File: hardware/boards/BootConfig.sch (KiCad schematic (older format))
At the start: 27 parts, among them J3 Conn_02x05_Odd_Even, SW1 SW_DIP_x03, U1 ECP5UM5G-381caBGA, U3 CYUSB3014, U5 128MiB

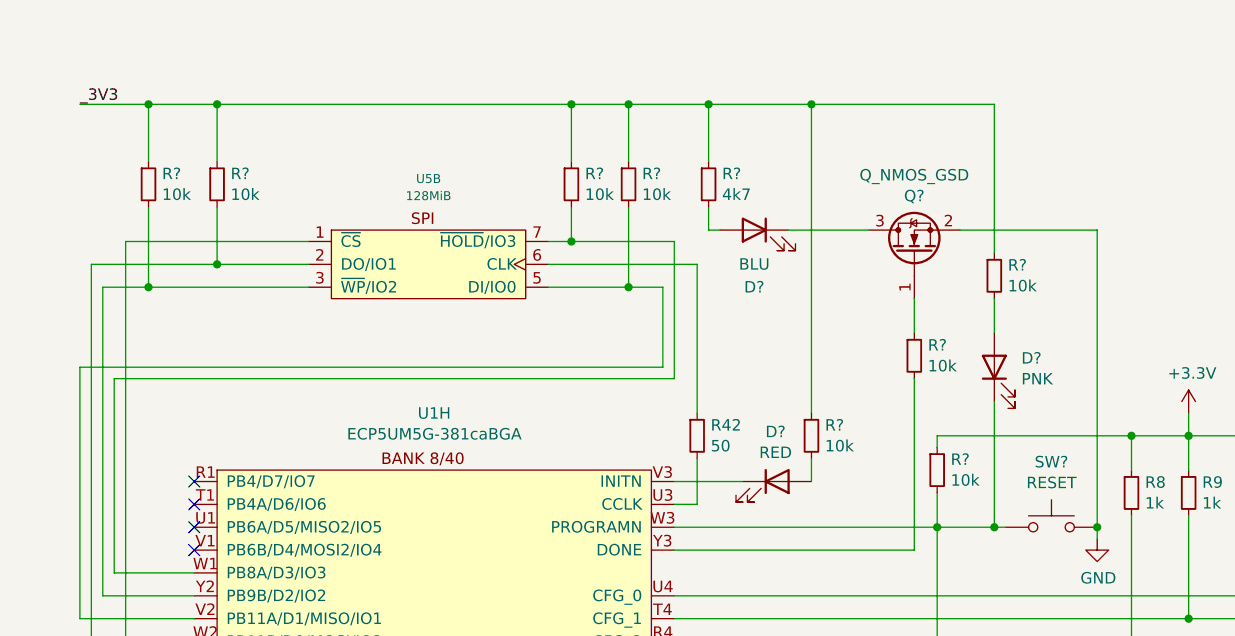
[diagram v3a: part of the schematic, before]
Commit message: Some ERC cleanup
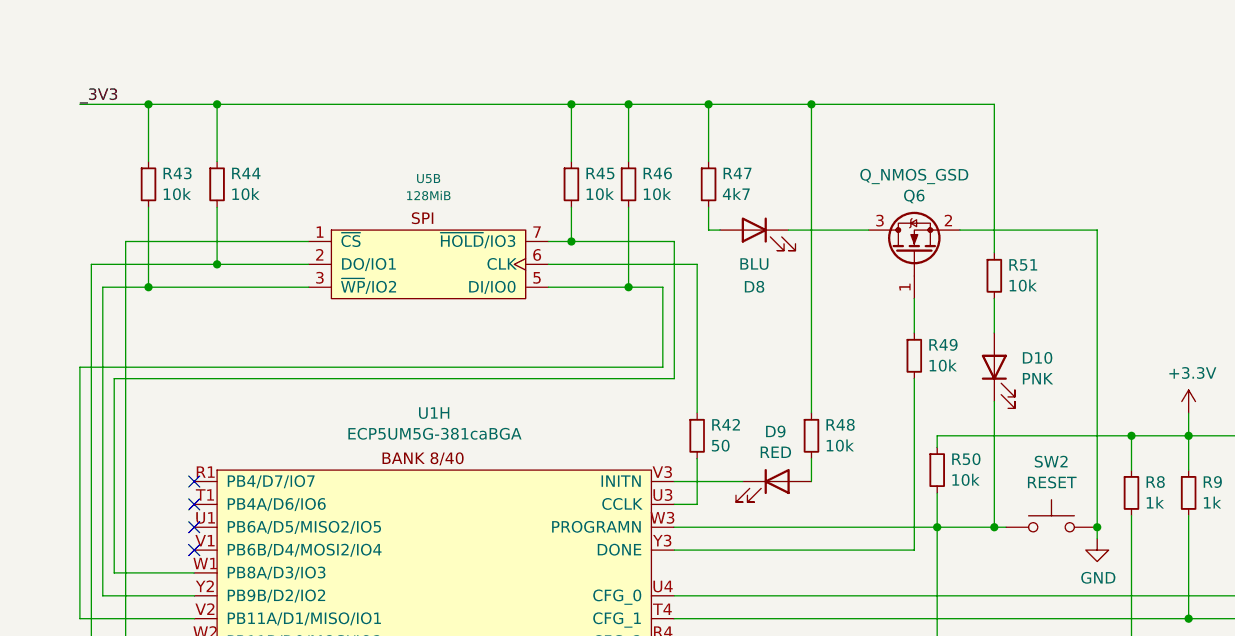
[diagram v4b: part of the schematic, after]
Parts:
- gave numbers to parts that had none: 14
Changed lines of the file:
@@
 	7400 4550 7400 4350
 $Comp
-L Switch:SW_Push SW?
+L Switch:SW_Push SW2
 U 1 1 5FFCED2D
 P 8950 4650
-F 0 "SW?" H 8950 4935 50  0000 C CNN
+F 0 "SW2" H 8950 4935 50  0000 C CNN
 F 1 "RESET" H 8950 4844 50  0000 C CNN
 F 2 "" H 8950 4850 50  0001 C CNN
@@
 P 5000 3150
 AR Path="/5EDF9F51/5FFF11C1" Ref="R?"  Part="1"
-AR Path="/5EF66251/5FFF11C1" Ref="R?"  Part="1"
-F 0 "R?" H 5059 3196 50  0000 L CNN
+AR Path="/5EF66251/5FFF11C1" Ref="R43"  Part="1"
+F 0 "R43" H 5059 3196 50  0000 L CNN
 F 1 "10k" H 5059 3105 50  0000 L CNN
 F 2 "Resistor_SMD:R_0603_1608Metric" H 5000 3150 50  0001 C CNN
@@
 P 5300 3150
 AR Path="/5EDF9F51/5FFF5085" Ref="R?"  Part="1"
-AR Path="/5EF66251/5FFF5085" Ref="R?"  Part="1"
-F 0 "R?" H 5359 3196 50  0000 L CNN
+AR Path="/5EF66251/5FFF5085" Ref="R44"  Part="1"
+F 0 "R44" H 5359 3196 50  0000 L CNN
 F 1 "10k" H 5359 3105 50  0000 L CNN
 F 2 "Resistor_SMD:R_0603_1608Metric" H 5300 3150 50  0001 C CNN
@@
 P 7100 3150
 AR Path="/5EDF9F51/5FFF5831" Ref="R?"  Part="1"
-AR Path="/5EF66251/5FFF5831" Ref="R?"  Part="1"
-F 0 "R?" H 7159 3196 50  0000 L CNN
+AR Path="/5EF66251/5FFF5831" Ref="R46"  Part="1"
+F 0 "R46" H 7159 3196 50  0000 L CNN
 F 1 "10k" H 7159 3105 50  0000 L CNN
 F 2 "Resistor_SMD:R_0603_1608Metric" H 7100 3150 50  0001 C CNN
@@
 P 6850 3150
 AR Path="/5EDF9F51/5FFF5FBB" Ref="R?"  Part="1"
-AR Path="/5EF66251/5FFF5FBB" Ref="R?"  Part="1"
-F 0 "R?" H 6909 3196 50  0000 L CNN
+AR Path="/5EF66251/5FFF5FBB" Ref="R45"  Part="1"
+F 0 "R45" H 6909 3196 50  0000 L CNN
 F 1 "10k" H 6909 3105 50  0000 L CNN
 F 2 "Resistor_SMD:R_0603_1608Metric" H 6850 3150 50  0001 C CNN
@@
 This should just be replaced with the proper\npull-ups/downs to statically configure,\nbut for rev 0 lets let it be configurable.
 $Comp
-L power:GND #PWR?
+L power:GND #PWR0128
 U 1 1 6021C990
 P 9150 4700
-F 0 "#PWR?" H 9150 4450 50  0001 C CNN
+F 0 "#PWR0128" H 9150 4450 50  0001 C CNN
 F 1 "GND" H 9155 4527 50  0000 C CNN
 F 2 "" H 9150 4700 50  0001 C CNN
@@
 P 8450 4400
 AR Path="/5EDF9F51/6022837B" Ref="R?"  Part="1"
-AR Path="/5EF66251/6022837B" Ref="R?"  Part="1"
-F 0 "R?" H 8509 4446 50  0000 L CNN
+AR Path="/5EF66251/6022837B" Ref="R50"  Part="1"
+F 0 "R50" H 8509 4446 50  0000 L CNN
 F 1 "10k" H 8509 4355 50  0000 L CNN
 F 2 "Resistor_SMD:R_0603_1608Metric" H 8450 4400 50  0001 C CNN
@@
 Connection ~ 9300 4250
 $Comp
-L Device:LED D?
+L Device:LED D10
 U 1 1 6023CC12
 P 8700 3950
-F 0 "D?" V 8739 3832 50  0000 R CNN
+F 0 "D10" V 8739 3832 50  0000 R CNN
 F 1 "PNK" V 8648 3832 50  0000 R CNN
 F 2 "LED_SMD:LED_0603_1608Metric" H 8700 3950 50  0001 C CNN
@@
 P 8700 3550
 AR Path="/5EDF9F51/6025A141" Ref="R?"  Part="1"
-AR Path="/5EF66251/6025A141" Ref="R?"  Part="1"
-F 0 "R?" H 8759 3596 50  0000 L CNN
+AR Path="/5EF66251/6025A141" Ref="R51"  Part="1"
+F 0 "R51" H 8759 3596 50  0000 L CNN
 F 1 "10k" H 8759 3505 50  0000 L CNN
 F 2 "Resistor_SMD:R_0603_1608Metric" H 8700 3550 50  0001 C CNN
@@
 Connection ~ 7100 2800
 $Comp
-L Device:LED D?
+L Device:LED D9
 U 1 1 60311968
 P 7750 4450
-F 0 "D?" H 7743 4667 50  0000 C CNN
+F 0 "D9" H 7743 4667 50  0000 C CNN
 F 1 "RED" H 7743 4576 50  0000 C CNN
 F 2 "LED_SMD:LED_0603_1608Metric" H 7750 4450 50  0001 C CNN
@@
 P 7900 4250
 AR Path="/5EDF9F51/60331B52" Ref="R?"  Part="1"
-AR Path="/5EF66251/60331B52" Ref="R?"  Part="1"
-F 0 "R?" H 7959 4296 50  0000 L CNN
+AR Path="/5EF66251/60331B52" Ref="R48"  Part="1"
+F 0 "R48" H 7959 4296 50  0000 L CNN
 F 1 "10k" H 7959 4205 50  0000 L CNN
 F 2 "Resistor_SMD:R_0603_1608Metric" H 7900 4250 50  0001 C CNN
@@
 P 8350 3450
 AR Path="/5EDF9F51/6036E4C5" Ref="Q?"  Part="1"
-AR Path="/5EF66251/6036E4C5" Ref="Q?"  Part="1"
-F 0 "Q?" V 8599 3450 50  0000 C CNN
+AR Path="/5EF66251/6036E4C5" Ref="Q6"  Part="1"
+F 0 "Q6" V 8599 3450 50  0000 C CNN
 F 1 "Q_NMOS_GSD" V 8690 3450 50  0000 C CNN
 F 2 "Package_TO_SOT_SMD:SOT-23" H 8550 3550 50  0001 C CNN
@@
 Connection ~ 9150 4650
 $Comp
-L Device:LED D?
+L Device:LED D8
 U 1 1 603DB6B8
 P 7650 3350
-F 0 "D?" H 7650 3100 50  0000 C CNN
+F 0 "D8" H 7650 3100 50  0000 C CNN
 F 1 "BLU" H 7650 3200 50  0000 C CNN
 F 2 "LED_SMD:LED_0603_1608Metric" H 7650 3350 50  0001 C CNN
@@
 P 7450 3150
 AR Path="/5EDF9F51/603E9951" Ref="R?"  Part="1"
-AR Path="/5EF66251/603E9951" Ref="R?"  Part="1"
-F 0 "R?" H 7509 3196 50  0000 L CNN
+AR Path="/5EF66251/603E9951" Ref="R47"  Part="1"
+F 0 "R47" H 7509 3196 50  0000 L CNN
 F 1 "4k7" H 7509 3105 50  0000 L CNN
 F 2 "Resistor_SMD:R_0603_1608Metric" H 7450 3150 50  0001 C CNN
@@
 P 8350 3900
 AR Path="/5EDF9F51/604133D3" Ref="R?"  Part="1"
-AR Path="/5EF66251/604133D3" Ref="R?"  Part="1"
-F 0 "R?" H 8409 3946 50  0000 L CNN
+AR Path="/5EF66251/604133D3" Ref="R49"  Part="1"
+F 0 "R49" H 8409 3946 50  0000 L CNN
 F 1 "10k" H 8409 3855 50  0000 L CNN
 F 2 "Resistor_SMD:R_0603_1608Metric" H 8350 3900 50  0001 C CNN

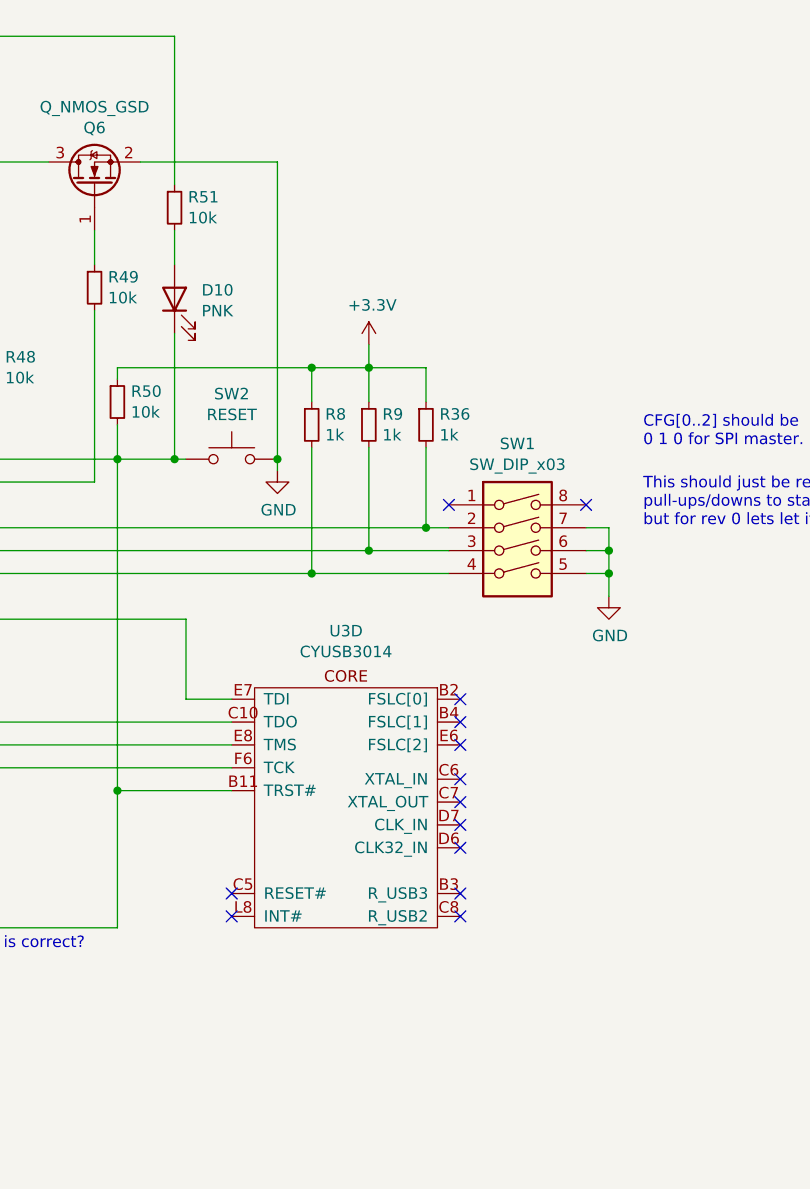
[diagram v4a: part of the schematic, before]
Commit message: Added a debounce cap to the reset switch, as well as selected the reset switch itself, also added the needed pull-down resistors for the USB PHY
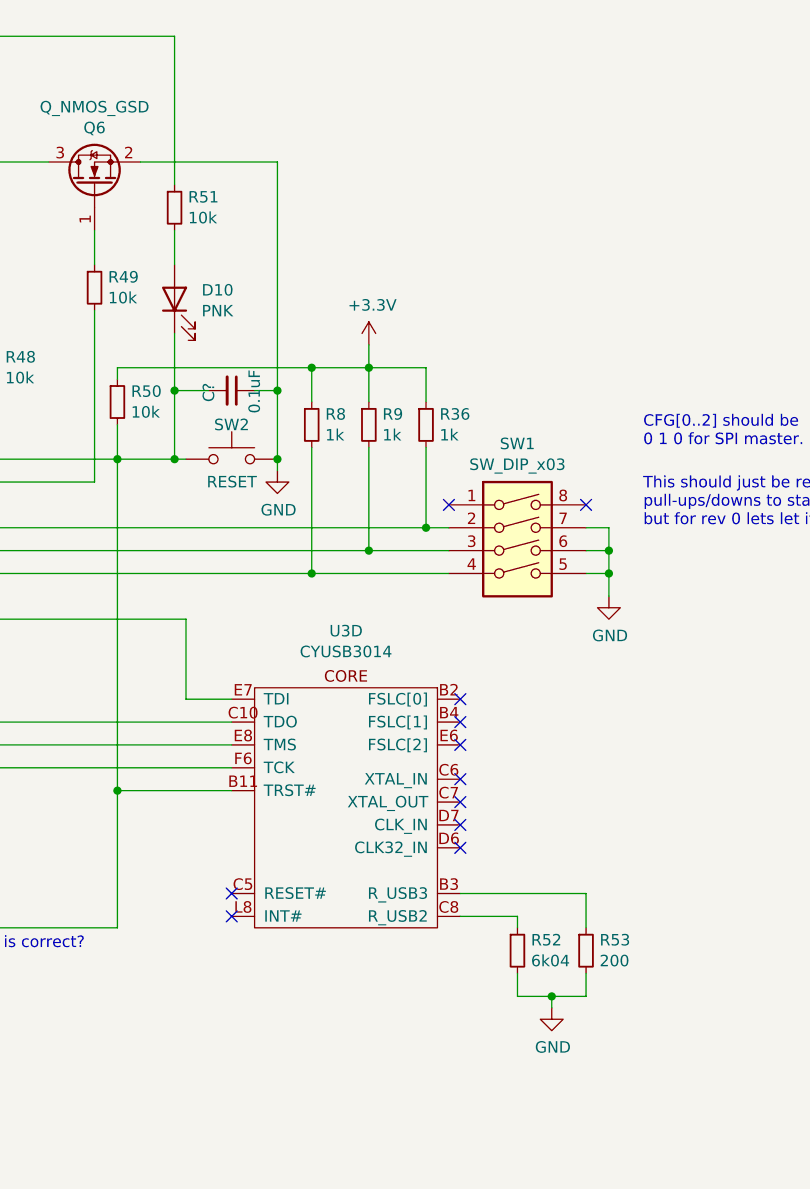
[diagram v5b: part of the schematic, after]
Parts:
- added C?: 0.1uF, Capacitor_SMD:C_0603_1608Metric, symbol Device:C_Small
- added R52: 6k04, Resistor_SMD:R_0603_1608Metric, symbol Device:R_Small
- added R53: 200, Resistor_SMD:R_0603_1608Metric, symbol Device:R_Small
- SW2: footprint (none) -> Button_Switch_SMD:SW_Push_1P1T_NO_CK_KMR2; MFR (none) -> C&K; MPN (none) -> KMR241NG ULC LFS
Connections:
- net GND: now also C?.1, R52.2, R53.2
- net at D10.1 (K), J3.10 (Pin_10), R50.2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: now also C?.2
- net at U3.B3 (R_USB3): now also R53.1
- net at U3.C8 (R_USB2): now also R52.1
- no-connect marks 22 -> 20
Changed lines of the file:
@@
 NoConn ~ 9950 6250
 NoConn ~ 9950 6350
-NoConn ~ 9950 6550
-NoConn ~ 9950 6650
 NoConn ~ 8950 6650
 NoConn ~ 8950 6550
@@
 U 1 1 5FFCED2D
 P 8950 4650
-F 0 "SW2" H 8950 4935 50  0000 C CNN
-F 1 "RESET" H 8950 4844 50  0000 C CNN
-F 2 "" H 8950 4850 50  0001 C CNN
-F 3 "~" H 8950 4850 50  0001 C CNN
+F 0 "SW2" H 8950 4800 50  0000 C CNN
+F 1 "RESET" H 8950 4550 50  0000 C CNN
+F 2 "Button_Switch_SMD:SW_Push_1P1T_NO_CK_KMR2" H 8950 4850 50  0001 C CNN
+F 3 "https://www.ckswitches.com/media/1479/kmr2.pdf" H 8950 4850 50  0001 C CNN
+F 4 "C&K" H 8950 4650 50  0001 C CNN "MFR"
+F 5 "KMR241NG ULC LFS" H 8950 4650 50  0001 C CNN "MPN"
 	1    8950 4650
 	1    0    0    -1
@@
 $EndComp
 Wire Wire Line
-	8700 4100 8700 4650
+	8700 4100 8700 4350
 Connection ~ 8700 4650
 Wire Wire Line
@@
 	8550 3350 9150 3350
 Wire Wire Line
-	9150 3350 9150 4650
+	9150 3350 9150 4350
 Connection ~ 9150 4650
 $Comp
@@
 Wire Wire Line
 	8450 6100 8450 4650
+$Comp
+L Device:R_Small R52
+U 1 1 60672CB4
+P 10200 6800
+F 0 "R52" H 10259 6846 50  0000 L CNN
+F 1 "6k04" H 10259 6755 50  0000 L CNN
+F 2 "Resistor_SMD:R_0603_1608Metric" H 10200 6800 50  0001 C CNN
+F 3 "~" H 10200 6800 50  0001 C CNN
+F 4 "Vishay Dale" H 10200 6800 50  0001 C CNN "MFR"
+F 5 "RCS06036K04FKEA" H 10200 6800 50  0001 C CNN "MPN"
+	1    10200 6800
+	1    0    0    -1
+$EndComp
+$Comp
+L Device:R_Small R53
+U 1 1 6067E54E
+P 10500 6800
+F 0 "R53" H 10559 6846 50  0000 L CNN
+F 1 "200" H 10559 6755 50  0000 L CNN
+F 2 "Resistor_SMD:R_0603_1608Metric" H 10500 6800 50  0001 C CNN
+F 3 "~" H 10500 6800 50  0001 C CNN
+F 4 "Vishay Dale" H 10500 6800 50  0001 C CNN "MFR"
+F 5 "RCS0603200RFKEA" H 10500 6800 50  0001 C CNN "MPN"
+	1    10500 6800
+	1    0    0    -1
+$EndComp
+Wire Wire Line
+	9950 6650 10200 6650
+Wire Wire Line
+	10200 6650 10200 6700
+Wire Wire Line
+	9950 6550 10500 6550
+Wire Wire Line
+	10500 6550 10500 6700
+$Comp
+L power:GND #PWR0129
+U 1 1 6068AA91
+P 10350 7050
+F 0 "#PWR0129" H 10350 6800 50  0001 C CNN
+F 1 "GND" H 10355 6877 50  0000 C CNN
+F 2 "" H 10350 7050 50  0001 C CNN
+F 3 "" H 10350 7050 50  0001 C CNN
+	1    10350 7050
+	1    0    0    -1
+$EndComp
+Wire Wire Line
+	10200 6900 10200 7000
+Wire Wire Line
+	10200 7000 10350 7000
+Wire Wire Line
+	10350 7000 10350 7050
+Wire Wire Line
+	10500 6900 10500 7000
+Wire Wire Line
+	10500 7000 10350 7000
+Connection ~ 10350 7000
+$Comp
+L Device:C_Small C?
+U 1 1 606E230C
+P 8950 4350
+AR Path="/5EDF9F51/606E230C" Ref="C?"  Part="1"
+AR Path="/5EF66251/606E230C" Ref="C?"  Part="1"
+F 0 "C?" H 9000 4250 50  0000 R CNN
+F 1 "0.1uF" H 9050 4450 50  0000 R CNN
+F 2 "Capacitor_SMD:C_0603_1608Metric" H 8950 4350 50  0001 C CNN
+F 3 "~" H 8950 4350 50  0001 C CNN
+F 4 "KEMET" V 8950 4350 50  0001 C CNN "MFR"
+F 5 "C0603C104M5RACTU" V 8950 4350 50  0001 C CNN "MPN"
+	1    8950 4350
+	0    1    1    0
+$EndComp
+Wire Wire Line
+	8700 4350 8850 4350
+Connection ~ 8700 4350
+Wire Wire Line
+	8700 4350 8700 4650
+Wire Wire Line
+	9050 4350 9150 4350
+Connection ~ 9150 4350
+Wire Wire Line
+	9150 4350 9150 4650
 $EndSCHEMATC

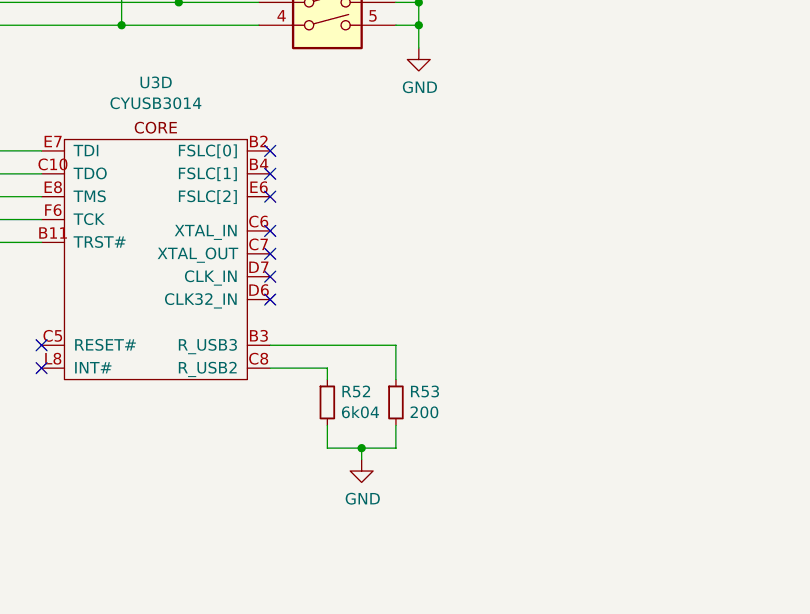
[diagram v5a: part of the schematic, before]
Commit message: Added the crystal for the USB PHY
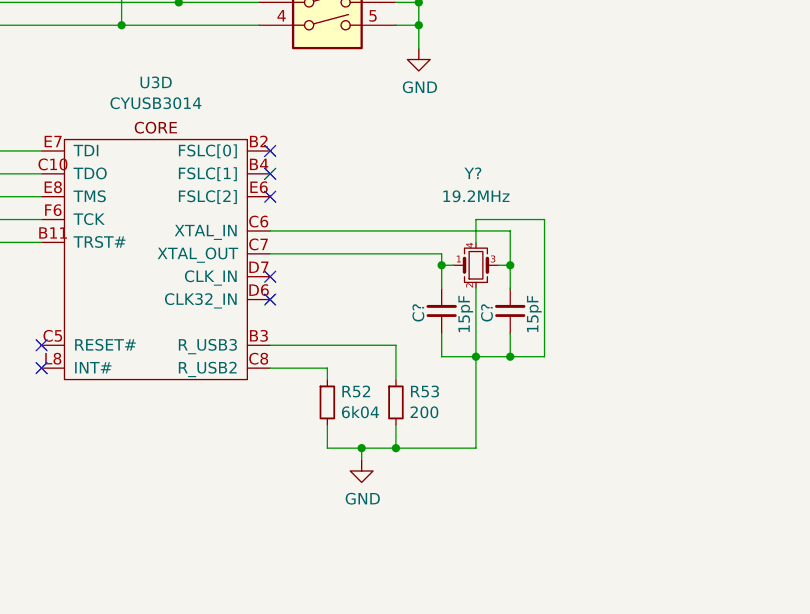
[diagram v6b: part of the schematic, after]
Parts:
- added C? (x2): 15pF, Capacitor_SMD:C_0603_1608Metric, symbol Device:C_Small
- added Y?: 19.2MHz, Crystal:Crystal_SMD_Abracon_ABM10-4Pin_2.5x2.0mm, symbol Device:Crystal_GND24_Small
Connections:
- net GND: now also C?.1, C?.1, Y?.2, Y?.4
- net at U3.C6 (XTAL_IN): now also C?.2, Y?.3
- net at U3.C7 (XTAL_OUT): now also C?.2, Y?.1
- no-connect marks 20 -> 18
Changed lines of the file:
@@
 NoConn ~ 9950 5800
 NoConn ~ 9950 5900
-NoConn ~ 9950 6050
-NoConn ~ 9950 6150
 NoConn ~ 9950 6250
 NoConn ~ 9950 6350
@@
 Wire Wire Line
 	9150 4350 9150 4650
+$Comp
+L Device:Crystal_GND24_Small Y?
+U 1 1 6071D344
+P 10850 6200
+F 0 "Y?" H 10800 6600 50  0000 L CNN
+F 1 "19.2MHz" H 10700 6500 50  0000 L CNN
+F 2 "Crystal:Crystal_SMD_Abracon_ABM10-4Pin_2.5x2.0mm" H 10850 6200 50  0001 C CNN
+F 3 "~" H 10850 6200 50  0001 C CNN
+F 4 "Abracon LLC" H 10850 6200 50  0001 C CNN "MFR"
+F 5 "ABM10-19.200MHZ-D30-T3" H 10850 6200 50  0001 C CNN "MPN"
+	1    10850 6200
+	1    0    0    -1
+$EndComp
+$Comp
+L Device:C_Small C?
+U 1 1 60727D1B
+P 10700 6400
+AR Path="/5EDF9F51/60727D1B" Ref="C?"  Part="1"
+AR Path="/5EF66251/60727D1B" Ref="C?"  Part="1"
+F 0 "C?" V 10800 6450 50  0000 R CNN
+F 1 "15pF" V 10600 6500 50  0000 R CNN
+F 2 "Capacitor_SMD:C_0603_1608Metric" H 10700 6400 50  0001 C CNN
+F 3 "~" H 10700 6400 50  0001 C CNN
+F 4 "KEMET" V 10700 6400 50  0001 C CNN "MFR"
+F 5 "C0603C150J5GACTU" V 10700 6400 50  0001 C CNN "MPN"
+	1    10700 6400
+	-1   0    0    1
+$EndComp
+$Comp
+L Device:C_Small C?
+U 1 1 607291D9
+P 11000 6400
+AR Path="/5EDF9F51/607291D9" Ref="C?"  Part="1"
+AR Path="/5EF66251/607291D9" Ref="C?"  Part="1"
+F 0 "C?" V 11100 6450 50  0000 R CNN
+F 1 "15pF" V 10900 6500 50  0000 R CNN
+F 2 "Capacitor_SMD:C_0603_1608Metric" H 11000 6400 50  0001 C CNN
+F 3 "~" H 11000 6400 50  0001 C CNN
+F 4 "KEMET" V 11000 6400 50  0001 C CNN "MFR"
+F 5 "C0603C150J5GACTU" V 11000 6400 50  0001 C CNN "MPN"
+	1    11000 6400
+	-1   0    0    1
+$EndComp
+Wire Wire Line
+	10750 6200 10700 6200
+Wire Wire Line
+	10700 6200 10700 6300
+Wire Wire Line
+	10950 6200 11000 6200
+Wire Wire Line
+	11000 6200 11000 6300
+Wire Wire Line
+	10500 7000 10850 7000
+Wire Wire Line
+	10850 6600 10700 6600
+Wire Wire Line
+	10700 6600 10700 6500
+Connection ~ 10500 7000
+Wire Wire Line
+	11000 6500 11000 6600
+Wire Wire Line
+	11000 6600 10850 6600
+Connection ~ 10850 6600
+Wire Wire Line
+	10850 6300 10850 6600
+Wire Wire Line
+	11150 6600 11000 6600
+Connection ~ 11000 6600
+Wire Wire Line
+	10850 6000 11150 6000
+Wire Wire Line
+	11150 6000 11150 6600
+Wire Wire Line
+	10850 6000 10850 6100
+Wire Wire Line
+	11000 6200 11000 6050
+Wire Wire Line
+	11000 6050 9950 6050
+Connection ~ 11000 6200
+Wire Wire Line
+	10850 7000 10850 6600
+Wire Wire Line
+	9950 6150 10700 6150
+Wire Wire Line
+	10700 6150 10700 6200
+Connection ~ 10700 6200
 $EndSCHEMATC
